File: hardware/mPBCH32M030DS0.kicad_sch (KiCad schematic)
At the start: 0 parts

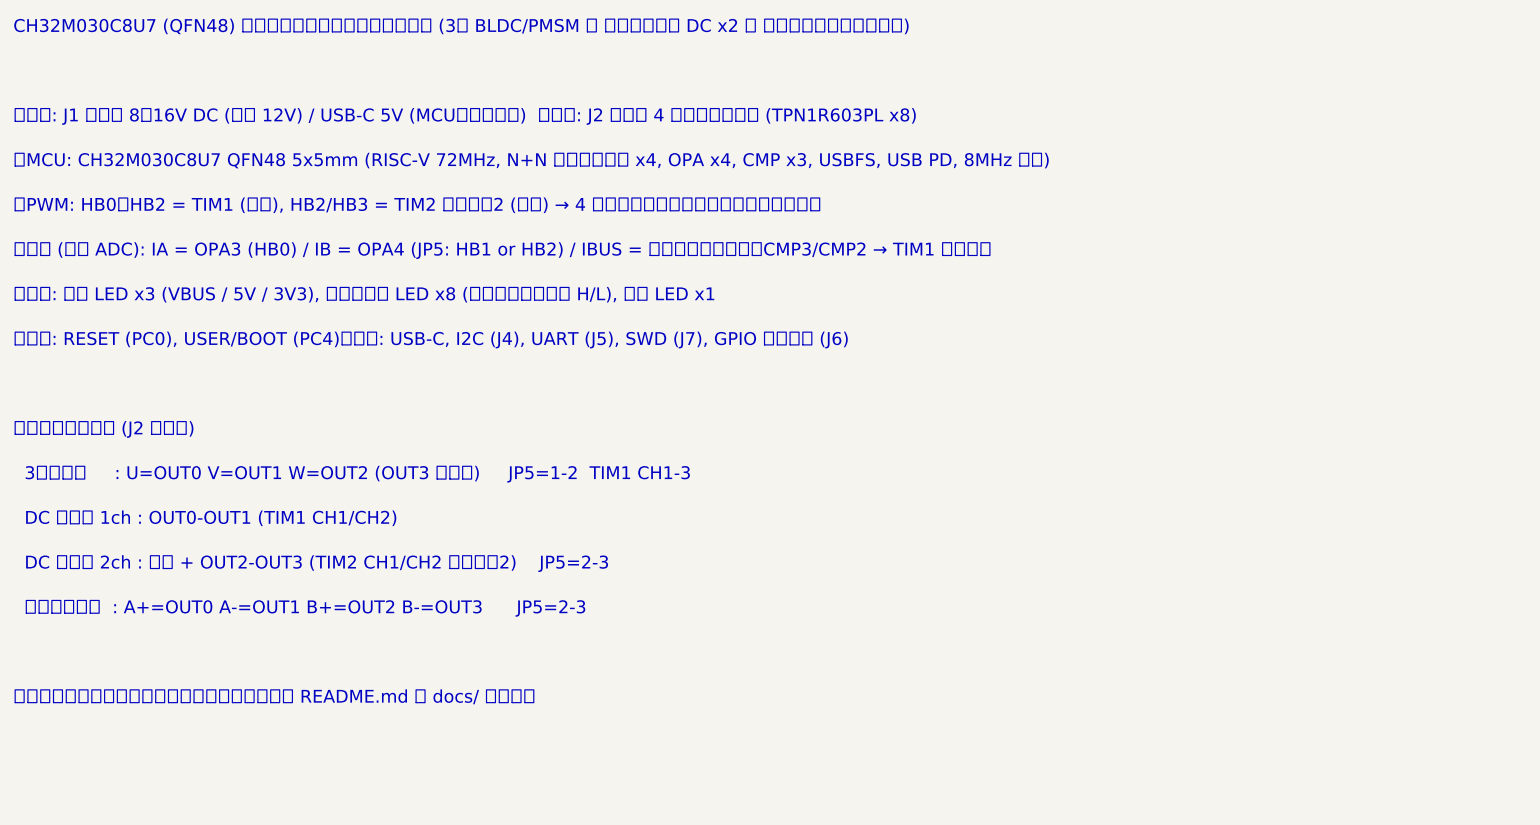
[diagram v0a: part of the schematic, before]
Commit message: Rev 0.2: 内蔵機能 (電流源/シンク・USB-PD・OPA/CMP 全モード) の活用
回路 (102/102 ネット一致):
- USB-PD シンクでモーター電源を供給: F3 → U5 LM74700 + Q10 → VBUS (PC3 で許可),
  USB VBUS 監視 (PA2), SMAJ20A。USBLC6 の基準を +3V3 に変更 (VBUS 20V 対策)
- J1 の逆接保護を U4 LM74700 + Q9 のハイサイド理想ダイオードに変更 (J1 / PD を安全に OR)
- 3 相センシングを PA5/PA6/PA7 に集約 (W 相 PA12 → PA6): CMP3 内部仮想中性点 + TIM2 捕捉
  によるセンサレス BEMF 検出, TIM2 ホール XOR, ISOURCE2 結線診断を同じピンで利用
- JP7: OPA3 入力を HB0 レッグ / バス電流で切替 (CMP2 + DAC でバス過電流・電流制限)
- JP8 + C105: QII1 (OPA1 → CMP1 → TIM3) でタコ / VR センサ / ブラシ DC 電流リップル計数
- 状態 LED を PC4 (USER/BOOT) と共用, J6/J7 を再割当 (1 線 SDI)

ファームウェア (警告 0):
- mpb.h ライブラリ: PD シンク (WCH USBPD_SNK 移植 + 8〜15V ポリシー + 給電パス制御),
  過電流保護 (CMP3/CMP2+DAC, TIM2 停止割込み), BEMF, ホール, タコ, NTC, 結線自己診断, TIM3 時間基準
- ブートローダ / テンプレートの状態 LED を PC4 (オープンドレイン) に変更

ドキュメント: docs/advanced_features.md (検討と判断, 要実機確認事項, Rev 0.3 候補)

Co-Authored-By: Claude Opus 5.5 <noreply@anthropic.com>
Claude-Session: https://claude.ai/code/session_01LENFjjhDfYjJZV1NWhB9uV
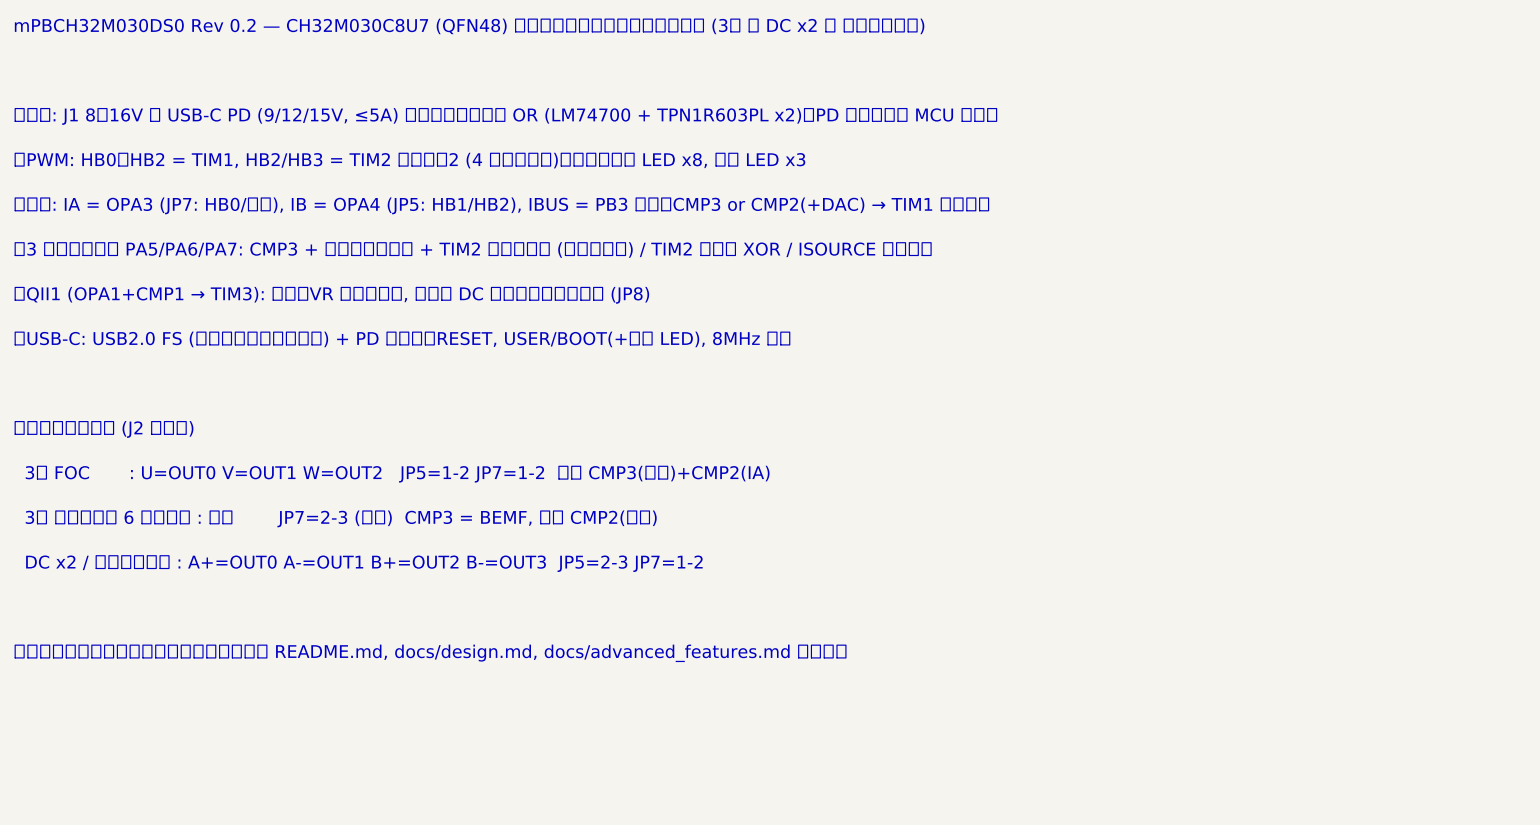
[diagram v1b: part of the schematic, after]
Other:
- note added: "3相 FOC : U=OUT0 V=OUT1 W=OUT2 JP5=1-2 JP7=1-2 保護 CMP3(バス)+CMP2(IA)"
- note added: "3相 センサレス 6 ステップ : 同上 JP7=2-3 (バス) CMP3 = BEMF, 保護 CMP2(バス)"
- note added: "DC x2 / ステッピング : A+=OUT0 A-=OUT1 B+=OUT2 B-=OUT3 JP5=2-3 JP7=1-2"
- note added: "mPBCH32M030DS0 Rev 0.2 — CH32M030C8U7 (QFN48) ユニバーサル・モータードライバ (3相 ・ DC x2 ・ ステッピング)"
- note added: "・3 相センシング PA5/PA6/PA7: CMP3 + 内部仮想中性点 + TIM2 キャプチャ (センサレス) / TIM2 ホール XOR / ISOURCE 自己診断"
- note added: "・PWM: HB0〜HB2 = TIM1, HB2/HB3 = TIM2 リマップ2 (4 レッグ相補)。ゲート確認 LED x8, 電源 LED x3"
- note added: "・QII1 (OPA1+CMP1 → TIM3): タコ・VR センサ入力, ブラシ DC の電流リップル計数 (JP8)"
- note added: "・USB-C: USB2.0 FS (ブートローダ書き込み) + PD シンク。RESET, USER/BOOT(+状態 LED), 8MHz 水晶"
- note added: "・電流: IA = OPA3 (JP7: HB0/バス), IB = OPA4 (JP5: HB1/HB2), IBUS = PB3 直接。CMP3 or CMP2(+DAC) → TIM1 ブレーキ"
- note added: "・電源: J1 8〜16V と USB-C PD (9/12/15V, ≤5A) を理想ダイオード OR (LM74700 + TPN1R603PL x2)。PD は契約後に MCU が許可"
- note added: "詳細設計・部品選定・内蔵機能の活用検討は README.md, docs/design.md, docs/advanced_features.md を参照。"
- note removed: "3相モータ : U=OUT0 V=OUT1 W=OUT2 (OUT3 未使用) JP5=1-2 TIM1 CH1-3"
- note removed: "CH32M030C8U7 (QFN48) ユニバーサル・モータードライバ (3相 BLDC/PMSM ・ フルブリッジ DC x2 ・ バイポーラステッピング)"
- note removed: "DC モータ 1ch : OUT0-OUT1 (TIM1 CH1/CH2)"
- note removed: "DC モータ 2ch : 上記 + OUT2-OUT3 (TIM2 CH1/CH2 リマップ2) JP5=2-3"
- note removed: "ステッピング : A+=OUT0 A-=OUT1 B+=OUT2 B-=OUT3 JP5=2-3"
- note removed: "・MCU: CH32M030C8U7 QFN48 5x5mm (RISC-V 72MHz, N+N プリドライバ x4, OPA x4, CMP x3, USBFS, USB PD, 8MHz 水晶)"
- note removed: "・PWM: HB0〜HB2 = TIM1 (相補), HB2/HB3 = TIM2 リマップ2 (相補) → 4 レッグすべてデッドタイム付き相補駆動"
- note removed: "・入力: J1 端子台 8〜16V DC (公称 12V) / USB-C 5V (MCU・通信のみ) ・出力: J2 端子台 4 ハーフブリッジ (TPN1R603PL x8)"
- note removed: "・操作: RESET (PC0), USER/BOOT (PC4)。通信: USB-C, I2C (J4), UART (J5), SWD (J7), GPIO 引き出し (J6)"
- note removed: "・表示: 電源 LED x3 (VBUS / 5V / 3V3), ゲート確認 LED x8 (各ハーフブリッジ H/L), 状態 LED x1"
- note removed: "・電流 (内蔵 ADC): IA = OPA3 (HB0) / IB = OPA4 (JP5: HB1 or HB2) / IBUS = バスシャント直接。CMP3/CMP2 → TIM1 ブレーキ"
- note removed: "詳細設計・部品選定・ピン割当・ブートローダは README.md と docs/ を参照。"
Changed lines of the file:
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@@
 (kicad_sch (version 20230121) (generator eeschema)
 (paper "A3")
-(title_block (title "mPBCH32M030DS0  CH32M030 Universal Motor Driver") (date "2026-09-24") (rev "0.1") (company "ghostinkoma") (comment 1 "トップシート / 仕様概要") (comment 2 "個人利用可 (クレジット表示必須) / 商用利用は要連絡 / 無保証  -  LICENSE 参照"))
-(text "CH32M030C8U7 (QFN48) ユニバーサル・モータードライバ (3相 BLDC/PMSM ・ フルブリッジ DC x2 ・ バイポーラステッピング)" (at 20 30 0) (effects (font (size 2 2)) (justify left bottom)))
+(title_block (title "mPBCH32M030DS0  CH32M030 Universal Motor Driver") (date "2026-09-24") (rev "0.2") (company "ghostinkoma") (comment 1 "トップシート / 仕様概要") (comment 2 "個人利用可 (クレジット表示必須) / 商用利用は要連絡 / 無保証  -  LICENSE 参照"))
+(text "mPBCH32M030DS0 Rev 0.2 — CH32M030C8U7 (QFN48) ユニバーサル・モータードライバ (3相 ・ DC x2 ・ ステッピング)" (at 20 30 0) (effects (font (size 2 2)) (justify left bottom)))
 (text "" (at 20 37 0) (effects (font (size 2 2)) (justify left bottom)))
-(text "・入力: J1 端子台 8〜16V DC (公称 12V) / USB-C 5V (MCU・通信のみ)  ・出力: J2 端子台 4 ハーフブリッジ (TPN1R603PL x8)" (at 20 44 0) (effects (font (size 2 2)) (justify left bottom)))
-(text "・MCU: CH32M030C8U7 QFN48 5x5mm (RISC-V 72MHz, N+N プリドライバ x4, OPA x4, CMP x3, USBFS, USB PD, 8MHz 水晶)" (at 20 51 0) (effects (font (size 2 2)) (justify left bottom)))
-(text "・PWM: HB0〜HB2 = TIM1 (相補), HB2/HB3 = TIM2 リマップ2 (相補) → 4 レッグすべてデッドタイム付き相補駆動" (at 20 58 0) (effects (font (size 2 2)) (justify left bottom)))
-(text "・電流 (内蔵 ADC): IA = OPA3 (HB0) / IB = OPA4 (JP5: HB1 or HB2) / IBUS = バスシャント直接。CMP3/CMP2 → TIM1 ブレーキ" (at 20 65 0) (effects (font (size 2 2)) (justify left bottom)))
-(text "・表示: 電源 LED x3 (VBUS / 5V / 3V3), ゲート確認 LED x8 (各ハーフブリッジ H/L), 状態 LED x1" (at 20 72 0) (effects (font (size 2 2)) (justify left bottom)))
-(text "・操作: RESET (PC0), USER/BOOT (PC4)。通信: USB-C, I2C (J4), UART (J5), SWD (J7), GPIO 引き出し (J6)" (at 20 79 0) (effects (font (size 2 2)) (justify left bottom)))
+(text "・電源: J1 8〜16V と USB-C PD (9/12/15V, ≤5A) を理想ダイオード OR (LM74700 + TPN1R603PL x2)。PD は契約後に MCU が許可" (at 20 44 0) (effects (font (size 2 2)) (justify left bottom)))
+(text "・PWM: HB0〜HB2 = TIM1, HB2/HB3 = TIM2 リマップ2 (4 レッグ相補)。ゲート確認 LED x8, 電源 LED x3" (at 20 51 0) (effects (font (size 2 2)) (justify left bottom)))
+(text "・電流: IA = OPA3 (JP7: HB0/バス), IB = OPA4 (JP5: HB1/HB2), IBUS = PB3 直接。CMP3 or CMP2(+DAC) → TIM1 ブレーキ" (at 20 58 0) (effects (font (size 2 2)) (justify left bottom)))
+(text "・3 相センシング PA5/PA6/PA7: CMP3 + 内部仮想中性点 + TIM2 キャプチャ (センサレス) / TIM2 ホール XOR / ISOURCE 自己診断" (at 20 65 0) (effects (font (size 2 2)) (justify left bottom)))
+(text "・QII1 (OPA1+CMP1 → TIM3): タコ・VR センサ入力, ブラシ DC の電流リップル計数 (JP8)" (at 20 72 0) (effects (font (size 2 2)) (justify left bottom)))
+(text "・USB-C: USB2.0 FS (ブートローダ書き込み) + PD シンク。RESET, USER/BOOT(+状態 LED), 8MHz 水晶" (at 20 79 0) (effects (font (size 2 2)) (justify left bottom)))
 (text "" (at 20 86 0) (effects (font (size 2 2)) (justify left bottom)))
 (text "駆動モード対応表 (J2 の結線)" (at 20 93 0) (effects (font (size 2 2)) (justify left bottom)))
-(text "  3相モータ     : U=OUT0 V=OUT1 W=OUT2 (OUT3 未使用)     JP5=1-2  TIM1 CH1-3" (at 20 100 0) (effects (font (size 2 2)) (justify left bottom)))
-(text "  DC モータ 1ch : OUT0-OUT1 (TIM1 CH1/CH2)" (at 20 107 0) (effects (font (size 2 2)) (justify left bottom)))
-(text "  DC モータ 2ch : 上記 + OUT2-OUT3 (TIM2 CH1/CH2 リマップ2)    JP5=2-3" (at 20 114 0) (effects (font (size 2 2)) (justify left bottom)))
-(text "  ステッピング  : A+=OUT0 A-=OUT1 B+=OUT2 B-=OUT3      JP5=2-3" (at 20 121 0) (effects (font (size 2 2)) (justify left bottom)))
-(text "" (at 20 128 0) (effects (font (size 2 2)) (justify left bottom)))
-(text "詳細設計・部品選定・ピン割当・ブートローダは README.md と docs/ を参照。" (at 20 135 0) (effects (font (size 2 2)) (justify left bottom)))
+(text "  3相 FOC       : U=OUT0 V=OUT1 W=OUT2   JP5=1-2 JP7=1-2  保護 CMP3(バス)+CMP2(IA)" (at 20 100 0) (effects (font (size 2 2)) (justify left bottom)))
+(text "  3相 センサレス 6 ステップ : 同上        JP7=2-3 (バス)  CMP3 = BEMF, 保護 CMP2(バス)" (at 20 107 0) (effects (font (size 2 2)) (justify left bottom)))
+(text "  DC x2 / ステッピング : A+=OUT0 A-=OUT1 B+=OUT2 B-=OUT3  JP5=2-3 JP7=1-2" (at 20 114 0) (effects (font (size 2 2)) (justify left bottom)))
+(text "" (at 20 121 0) (effects (font (size 2 2)) (justify left bottom)))
+(text "詳細設計・部品選定・内蔵機能の活用検討は README.md, docs/design.md, docs/advanced_features.md を参照。" (at 20 128 0) (effects (font (size 2 2)) (justify left bottom)))
 (sheet (at 20 160) (size 70 30) (fields_autoplaced) (stroke (width 0.1524) (type solid)) (fill (color 0 0 0 0.0000))
 (property "Sheetname" "電源入力・保護・補助電源・電源表示" (at 20 159.3 0) (effects (font (size 1.5 1.5)) (justify left bottom)))
